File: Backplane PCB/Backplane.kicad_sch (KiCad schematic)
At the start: 213 parts, among them J1 10018783-10202TLF, J2 10018783-10202TLF, J3 10018783-10202TLF, J4 10018783-10202TLF, J5 10018783-10202TLF, J6 5019514000, U1 LTC3894EFE-PBF, U10 ADP7104ACPZ-R7, U11 ISP817CXSM, U12 ISP817CXSM, U13 ISP817CXSM, U14 ISP817CXSM, U15 ISP817CXSM, U16 ISP817CXSM, U17 OP191GSZ-REEL7, U18 OP191GSZ-REEL7, U19 OP191GSZ-REEL7, U2 FDS4435A, U20 OP191GSZ-REEL7, U21 OP191GSZ-REEL7, U3 ISP817CXSM, U4 ISP817CXSM, U5 ISP817CXSM, U6 ISP817CXSM, U7 ISP817CXSM, U8 ISP817CXSM, U9 ADP7104ACPZ-R7

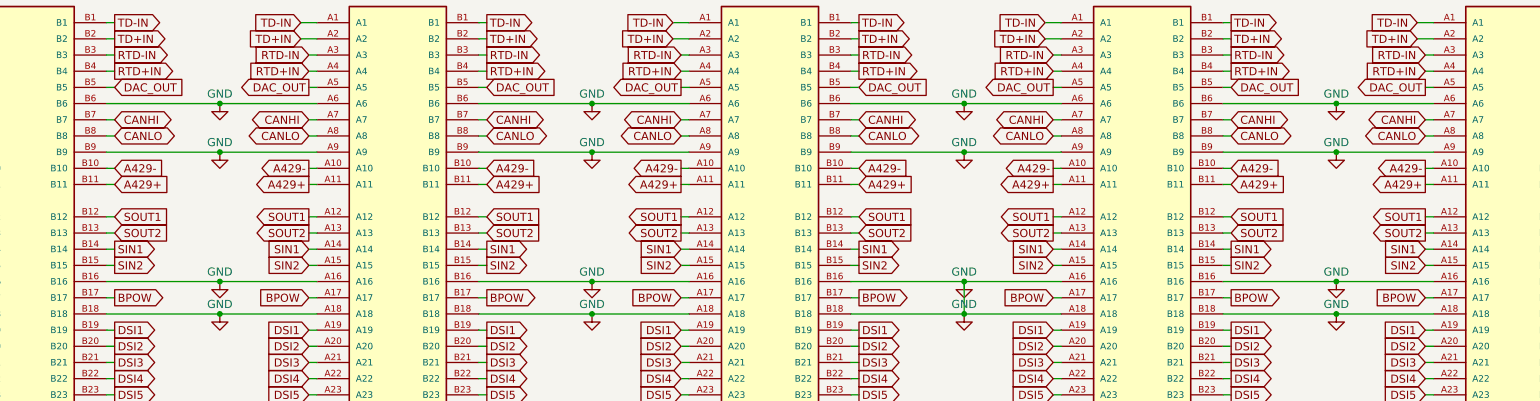
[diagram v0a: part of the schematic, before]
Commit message: Adjusted pins connections names
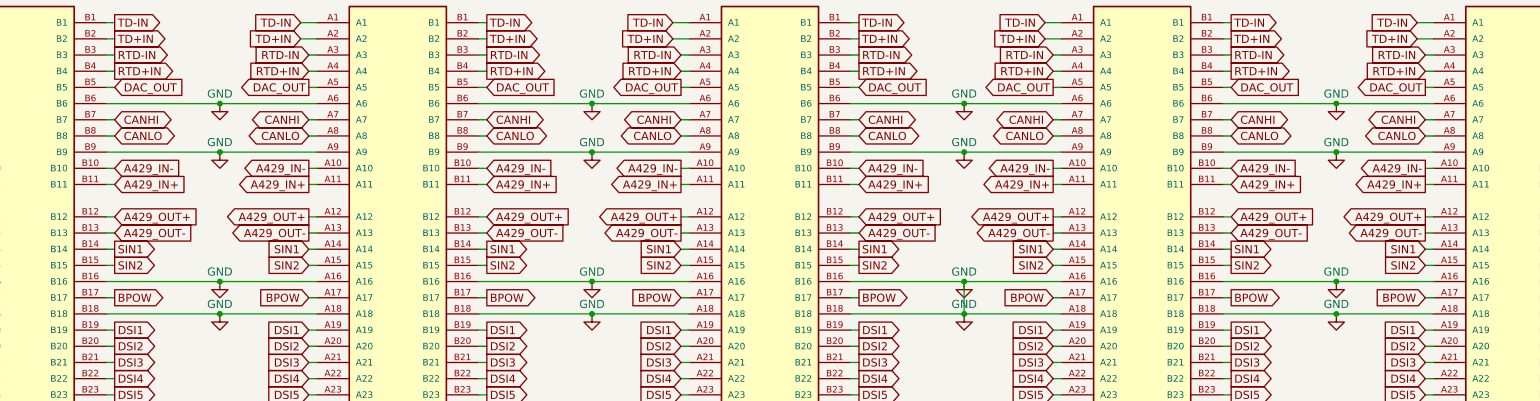
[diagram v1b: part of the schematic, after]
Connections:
- net A429+ is gone; now on net A429_IN+: J1.B11, J2.A11, J2.B11, J3.A11, J3.B11, J4.A11, J4.B11, J5.A11
- net A429- is gone; now on net A429_IN-: J1.B10, J2.A10, J2.B10, J3.A10, J3.B10, J4.A10, J4.B10, J5.A10
- net SOUT1 is gone; now on net A429_OUT+: J1.B12, J2.A12, J2.B12, J3.A12, J3.B12, J4.A12, J4.B12, J5.A12
- net SOUT2 is gone; now on net A429_OUT-: J1.B13, J2.A13, J2.B13, J3.A13, J3.B13, J4.A13, J4.B13, J5.A13

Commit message: Added logo
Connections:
- net A429_IN+: now also J5.B11
- net A429_IN-: now also J5.B10
- net A429_OUT+: now also J5.B12
- net A429_OUT-: now also J5.B13
- net BPOW: now also J5.B17
- net CANHI: now also J5.B7
- net CANLO: now also J5.B8
- net DAC_OUT: now also J5.B5
- net DOFB1: now also J5.B27
- net DOFB2: now also J5.B28
- net DOFB3: now also J5.B29
- net DOFB4: now also J5.B30
- net DOFB5: now also J5.B31
- net DOFB6: now also J5.B32
- net DSI1: now also J5.B19
- net DSI2: now also J5.B20
- net DSI3: now also J5.B21
- net DSI4: now also J5.B22
- net DSI5: now also J5.B23
- net DSI6: now also J5.B24
- net GND: now also J5.B16, J5.B18, J5.B25, J5.B26, J5.B6, J5.B9
- net RTD+IN: now also J5.B4
- net RTD-IN: now also J5.B3
- net SIN1: now also J5.B14
- net SIN2: now also J5.B15
- net TD+IN: now also J5.B2
- net TD-IN: now also J5.B1

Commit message: Changed K to k on resistors
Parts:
- R38, R39, R40, R41, R42, R43, R44, R45, R46, R47, R48, R49: value 1K -> 1k
- R5, R55, R56, R57, R58, R59, R60: value 10K -> 10k
- R50, R51, R52, R53: value 100K -> 100k
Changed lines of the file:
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@@
 			)
 		)
-		(property "Value" "100K"
+		(property "Value" "100k"
 			(at 48.26 72.39 90)
 			(effects
@@
 			)
 		)
-		(property "Value" "1K"
+		(property "Value" "1k"
 			(at 326.644 97.028 90)
 			(effects
@@
 			)
 		)
-		(property "Value" "1K"
+		(property "Value" "1k"
 			(at 388.62 142.24 90)
 			(effects
@@
 			)
 		)
-		(property "Value" "10K"
+		(property "Value" "10k"
 			(at 134.874 200.406 90)
 			(effects
@@
 			)
 		)
-		(property "Value" "1K"
+		(property "Value" "1k"
 			(at 327.914 183.388 90)
 			(effects
@@
 			)
 		)
-		(property "Value" "10K"
+		(property "Value" "10k"
 			(at 134.874 139.446 90)
 			(effects
@@
 			)
 		)
-		(property "Value" "10K"
+		(property "Value" "10k"
 			(at 195.58 101.6 90)
 			(effects
@@
 			)
 		)
-		(property "Value" "10K"
+		(property "Value" "10k"
 			(at 134.874 119.126 90)
 			(effects
@@
 			)
 		)
-		(property "Value" "1K"
+		(property "Value" "1k"
 			(at 388.62 97.79 90)
 			(effects
@@
 			)
 		)
-		(property "Value" "1K"
+		(property "Value" "1k"
 			(at 272.288 181.61 90)
 			(effects
@@
 			)
 		)
-		(property "Value" "100K"
+		(property "Value" "100k"
 			(at 45.72 231.14 90)
 			(effects
@@
 			)
 		)
-		(property "Value" "1K"
+		(property "Value" "1k"
 			(at 450.85 184.15 90)
 			(effects
@@
 			)
 		)
-		(property "Value" "100K"
+		(property "Value" "100k"
 			(at 44.45 304.8 90)
 			(effects
@@
 			)
 		)
-		(property "Value" "1K"
+		(property "Value" "1k"
 			(at 388.62 182.88 90)
 			(effects
@@
 			)
 		)
-		(property "Value" "1K"
+		(property "Value" "1k"
 			(at 327.914 141.732 90)
 			(effects
@@
 			)
 		)
-		(property "Value" "10K"
+		(property "Value" "10k"
 			(at 134.874 159.766 90)
 			(effects
@@
 			)
 		)
-		(property "Value" "10K"
+		(property "Value" "10k"
 			(at 134.874 98.806 90)
 			(effects
@@
 			)
 		)
-		(property "Value" "100K"
+		(property "Value" "100k"
 			(at 45.72 148.59 90)
 			(effects
@@
 			)
 		)
-		(property "Value" "1K"
+		(property "Value" "1k"
 			(at 270.51 139.7 90)
 			(effects
@@
 			)
 		)
-		(property "Value" "1K"
+		(property "Value" "1k"
 			(at 450.85 142.24 90)
 			(effects
@@
 			)
 		)
-		(property "Value" "1K"
+		(property "Value" "1k"
 			(at 273.05 97.282 90)
 			(effects
@@
 			)
 		)
-		(property "Value" "10K"
+		(property "Value" "10k"
 			(at 134.874 180.086 90)
 			(effects
@@
 			)
 		)
-		(property "Value" "1K"
+		(property "Value" "1k"
 			(at 450.85 97.79 90)
 			(effects

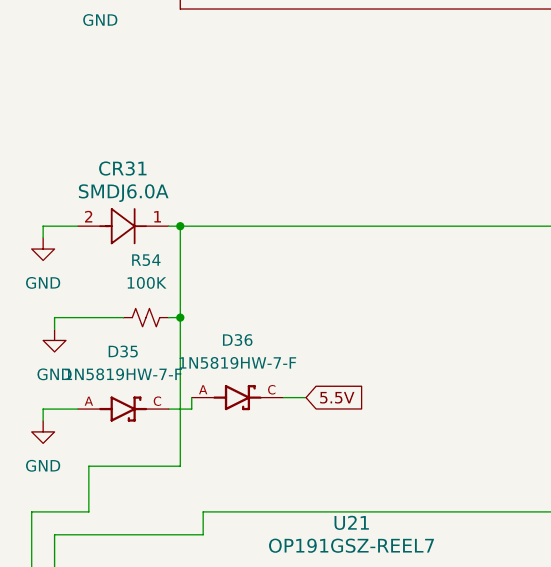
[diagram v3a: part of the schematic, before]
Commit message: Generated BOM and POS for backplane
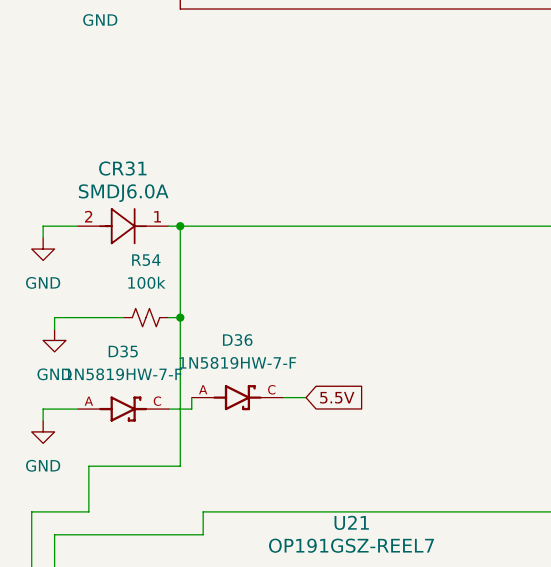
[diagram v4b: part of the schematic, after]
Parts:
- R54: value 100K -> 100k
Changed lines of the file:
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@@
 			)
 		)
-		(property "Value" "100K"
+		(property "Value" "100k"
 			(at 40.64 384.81 90)
 			(effects
